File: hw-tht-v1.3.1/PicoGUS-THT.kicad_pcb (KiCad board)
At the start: 2 copper layers, 103.7 x 99.8 mm, 83 parts, among them J1 IRQDMA_JP, J10 GY-PCM5102, J3 Bus_ISA_8bit, J5 SJ1-3535NG, J6 UART_TX, J7 USB power jumper, J8 SJ1-3535NG-GR, J9 Waveblaster, U1 Pico, U10 74AHCT126, U11 NE5532, U2 74AHC244, U3 SN74CB3T3257, U4 SN74CB3T3257, U5 74AHC14, U6 74AHC00, U7 74AHC00, U8 APS6404L-3SQR-SN, U9 PCM5100A

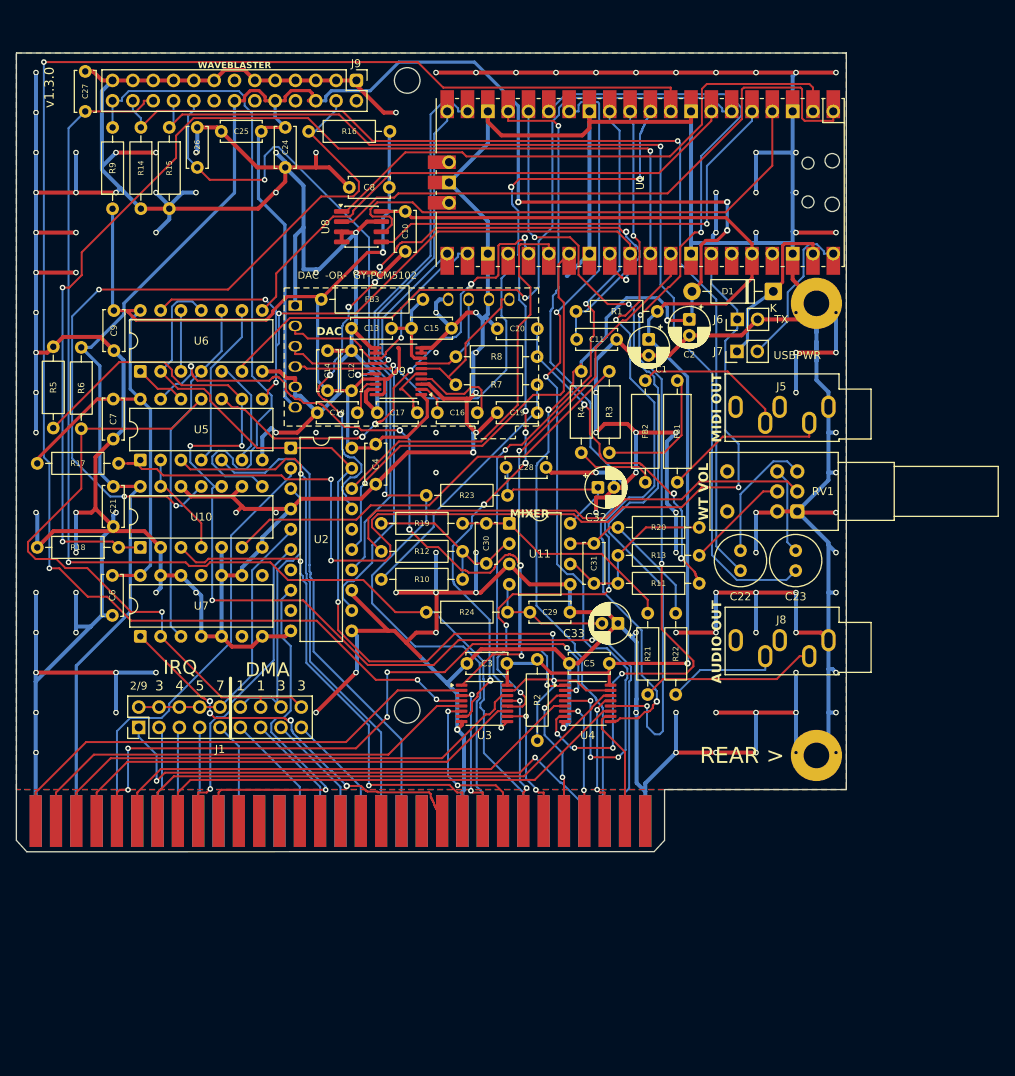
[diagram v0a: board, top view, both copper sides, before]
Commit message: THT rev B: dual USB-A/USB-C footprint, unrouted v1.3.1 board
- J11 footprint USB_A_C_Dual_Molex_67643_GCT_USB4085_Horizontal: Molex 67643
  USB-A or GCT USB4085 USB-C (all THT), both centred on one line, front faces
  1.5 mm beyond the board edge
- project rules: min hole-to-hole 0.45 mm, min annular 0.12 mm for the
  USB4085 pins; PicoGUS-THT.kicad_dru keeps 0.50/0.13 mm everywhere else
- PicoGUS-THT.kicad_pcb: unrouted (tracks, vias and zone fills removed),
  v1.3.0 positions; U1 on RPi_Pico_SMD_TH_USB, U3/U4 on the nested footprint
  at their old centres (turned 90 deg), new parts parked below the ISA edge,
  J11 aligned to the bracket edge line; silkscreen v1.3.1
- schematic: J11 footprint, F1 Bourns MF-R050

Still to come: BOM, socket BOM, README.

Co-Authored-By: Claude Opus 5.5 <noreply@anthropic.com>
Claude-Session: https://claude.ai/code/session_011utN3x8yYUNDvkpGCEq5yD
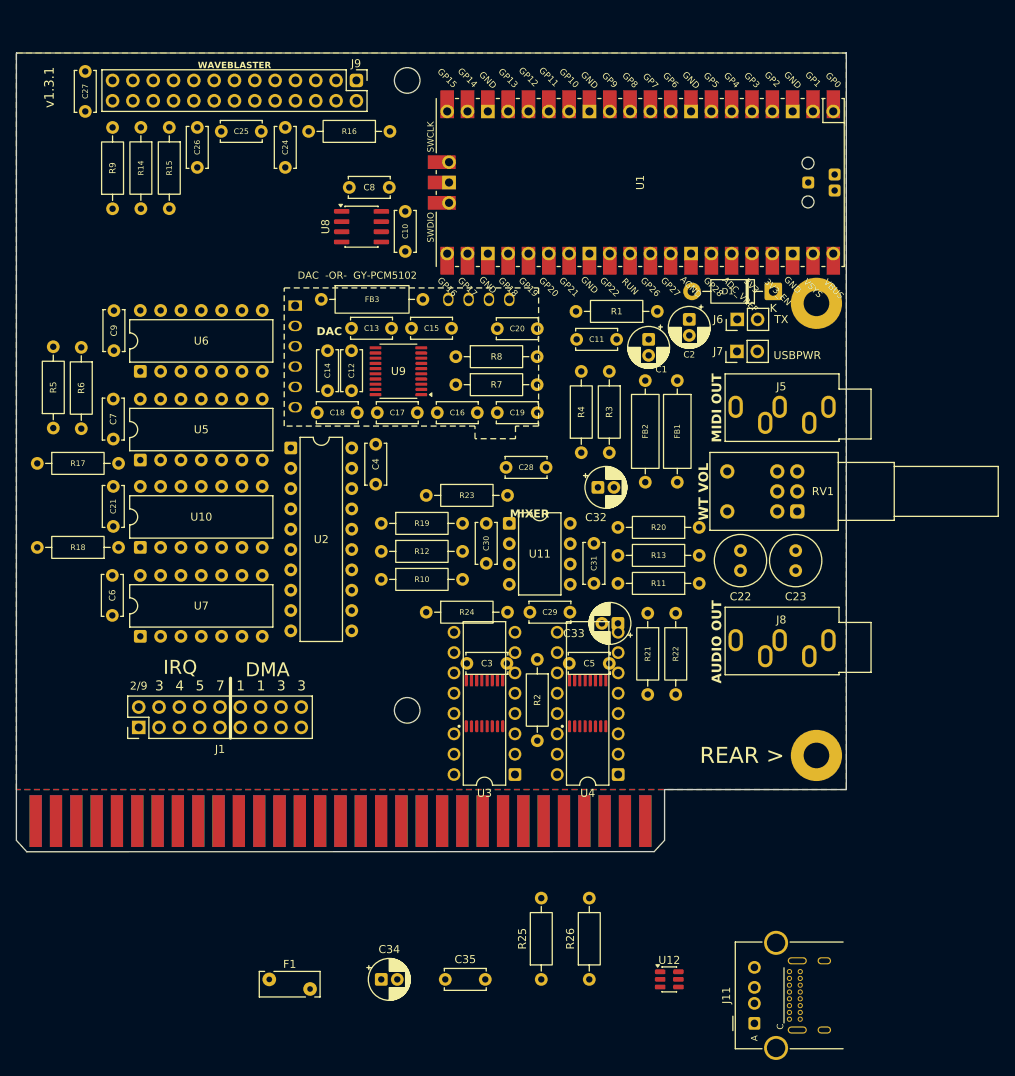
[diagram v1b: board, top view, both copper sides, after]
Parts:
- added C34: 47uF, Capacitor_THT:CP_Radial_D5.0mm_P2.00mm, F.Cu at (162.0, 152.0)
- added C35: 0.1uF, Capacitor_THT:C_Disc_D5.0mm_W2.5mm_P5.00mm, F.Cu at (170.0, 152.0)
- added F1: 0.5A PTC, Fuse:Fuse_Bourns_MF-RHT050, F.Cu at (148.0, 152.0)
- added J11: USB-A or USB-C, PiGUS library:USB_A_C_Dual_Molex_67643_GCT_USB4085_Horizontal, F.Cu at (220.1, 154.0)
- added R25: 56K, Resistor_THT:R_Axial_DIN0207_L6.3mm_D2.5mm_P10.16mm_Horizontal, F.Cu at (182.0, 152.0)
- added R26: 56K, Resistor_THT:R_Axial_DIN0207_L6.3mm_D2.5mm_P10.16mm_Horizontal, F.Cu at (188.0, 152.0)
- added U12: USBLC6-2SC6, Package_TO_SOT_SMD:SOT-23-6, F.Cu at (198.0, 152.0)
- U1: footprint PiGUS library:RPi_Pico_SMD_TH -> PiGUS library:RPi_Pico_SMD_TH_USB
- U3, U4: footprint Package_SO:TSSOP-16_4.4x5mm_P0.65mm -> PiGUS library:DIP-16_W7.62mm_TSSOP-16_Nested
- turned U3 to 90 degrees
- turned U4 to 90 degrees
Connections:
- J10 pad 13: /PCM5100 audio/DAC_OUTR -> /PCM5100 audio/AUDIO_R
- J10 pad 15: /PCM5100 audio/DAC_OUTL -> /PCM5100 audio/AUDIO_L
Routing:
- net GND: track 1290.5 -> 0.00 mm, vias 131 -> 0
- net +5V: track 335.3 -> 0.00 mm, vias 5 -> 0
- net +3V3: track 317.7 -> 0.00 mm, vias 2 -> 0
- net AD0: track 204.6 -> 0.00 mm, vias 4 -> 0
- net ADS: track 156.5 -> 0.00 mm, vias 7 -> 0
- net -12V: track 146.3 -> 0.00 mm, vias 1 -> 0
- net ~{RI/OCHRDY}: track 141.9 -> 0.00 mm, vias 3 -> 0
- net RESET: track 141.2 -> 0.00 mm, vias 4 -> 0
- net AD5: track 134.1 -> 0.00 mm, vias 7 -> 0
- net /Wavetable & line out/WT_R: track 133.3 -> 0.00 mm, vias 1 -> 0
- net UART_TX: track 132.5 -> 0.00 mm, vias 3 -> 0
- net +12V: track 130.8 -> 0.00 mm, vias 2 -> 0
- net /Wavetable & line out/WT_L: track 130.2 -> 0.00 mm, vias 1 -> 0
- net ~{BUSOE}: track 121.6 -> 0.00 mm, vias 3 -> 0
- net AD4: track 109.7 -> 0.00 mm, vias 5 -> 0
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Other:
- board text added: "PicoGUS v1.3.1 © 2023-2026 Ian Scott (polpo), Vidar Waagbø (waagbo) Licensed under CERN-OHL-P v2 https://github.com/waagbo/picogus Thanks to all the people that have contributed over the years!"
- board text added: "rev B (v1.3.1) new parts, to be placed: J11 USB-A/C: origin on the bracket edge line, rot 90 (aligned already) F1, C34, C35 near J11; R25/R26 USB-C CC; U12 ESD (optional)"
- board text added: "v1.3.1"
- board text removed: "PicoGUS v1.3.0 © 2023-2026 Ian Scott (polpo), Vidar Waagbø (waagbo) Licensed under CERN-OHL-P v2 https://github.com/waagbo/picogus Thanks to all the people that have contributed over the years!"
- board text removed: "v1.3.0"

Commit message: THT rev B: review fixes, C34 220uF, schematic PDF
Schematic
- C34 (USB VBUS bulk) 220 uF low-impedance Rubycon 16ZLH220MEFC6.3X11
  (USB 2.0 asks for >= 120 uF per host port)
- own UUID namespace for the rev B items (the USB sheet had reused UUIDs of
  v1.3.0 items, which mixed up ERC markers)
- TP1-TP3 pin names empty ("") in the embedded Pico_USB copy (KiCad 10 drew
  "~" literally)
- R25/R26 DigiKey/LCSC fields, U3/U4 adapter note (PA0034C first, BOB-13994
  has 0.635 mm pads), U12 in the title block's SMD list, USB sheet note
  reworded, USB-C always-on VBUS warning
- schematic PDF re-exported (4 pages)

Board
- U1: the library footprint's Pico pin-name/SWD silkscreen texts removed
  again (as in the v1.3.0 label clean-up)
- U3/U4 references back at their v1.3.0 spots (were on the gold fingers)
- U1, U3, U4 back in their footprint groups
- VBUS_USB in the pwr net class

BOM: C34 own line; BOM, uploads and socket BOM regenerated.

Co-Authored-By: Claude Opus 5.5 <noreply@anthropic.com>
Claude-Session: https://claude.ai/code/session_011utN3x8yYUNDvkpGCEq5yD
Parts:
- C34: value 47uF -> 220uF; footprint Capacitor_THT:CP_Radial_D5.0mm_P2.00mm -> Capacitor_THT:CP_Radial_D6.3mm_P2.50mm

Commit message: THT rev B: USB-A only for J11 (USB-C on hold)
- J11: Connector:USB_A on the stock Connector_USB:USB_A_Molex_67643_Horizontal
  (Molex 0676430910), parked with the flange 1.5 mm beyond the bracket edge
- R25/R26 (USB-C CC Rp) removed; design rules back to v1.3.0 (min hole-to-hole
  0.50 mm, annular 0.13 mm), PicoGUS-THT.kicad_dru removed
- the dual USB-A/USB-C footprint stays in the shared library, unused, for a
  possible USB-C option later
- BOM, DigiKey uploads, schematic PDF and README updated

Co-Authored-By: Claude Opus 5.5 <noreply@anthropic.com>
Claude-Session: https://claude.ai/code/session_011utN3x8yYUNDvkpGCEq5yD
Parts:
- removed R25, R26: 56K, Resistor_THT:R_Axial_DIN0207_L6.3mm_D2.5mm_P10.16mm_Horizontal
- J11: value USB-A or USB-C -> USB-A; footprint PiGUS library:USB_A_C_Dual_Molex_67643_GCT_USB4085_Horizontal -> Connector_USB:USB_A_Molex_67643_Horizontal
- moved U12 16.0 mm to (182.0, 152.0)
- moved J11 12.0 mm to (208.6, 157.5)
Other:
- board text added: "rev B (v1.3.1) new parts, to be placed: J11 USB-A: flange 1.5 mm beyond the bracket edge (aligned already) F1, C34, C35 near J11; U12 ESD (optional)"
- board text removed: "rev B (v1.3.1) new parts, to be placed: J11 USB-A/C: origin on the bracket edge line, rot 90 (aligned already) F1, C34, C35 near J11; R25/R26 USB-C CC; U12 ESD (optional)"

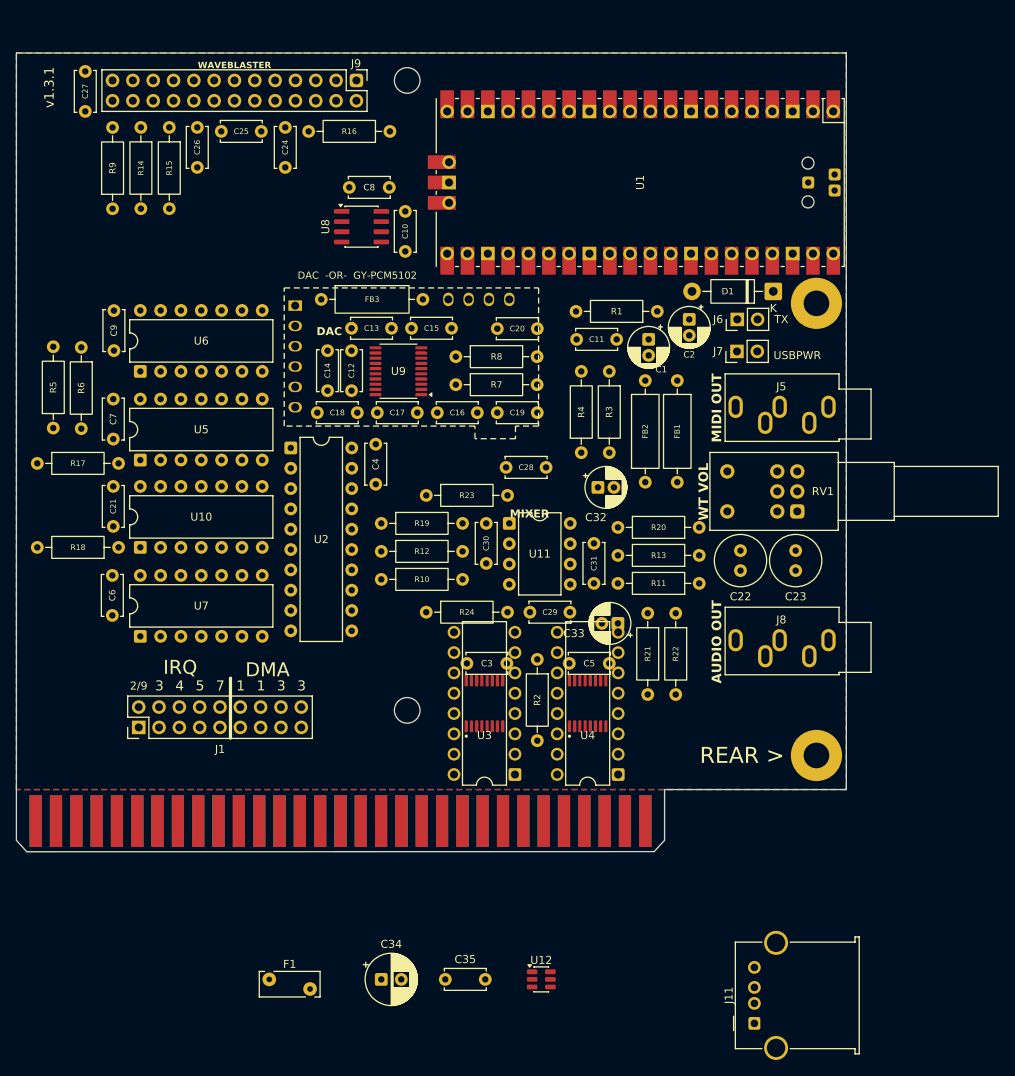
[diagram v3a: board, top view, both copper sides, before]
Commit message: THT rev B: user's new placement; USB port and Waveblaster standoff holes dropped
- PicoGUS-THT.kicad_pcb: the user's rev B placement (Pico moved down, bracket
  parts and mixer regrouped), unrouted
- USB host port removed again (usb.kicad_sch, J11, F1, C34, C35, U12); U1 back
  on the v1.3.0 Pico symbol and RPi_Pico_SMD_TH footprint
- J9 on the new Wavetable_NoMountingHoles footprint (no daughterboard standoff
  holes; the far one landed in U4); standoff and screws dropped from the BOM
- card outline: the 6.35 mm Edge.Cuts step at x 197.41 next to the ISA
  fingers had been dragged off the board in the upload; restored
- design rules identical to v1.3.0
- BOM, DigiKey uploads, socket BOM, schematic PDF and README updated

Co-Authored-By: Claude Opus 5.5 <noreply@anthropic.com>
Claude-Session: https://claude.ai/code/session_011utN3x8yYUNDvkpGCEq5yD
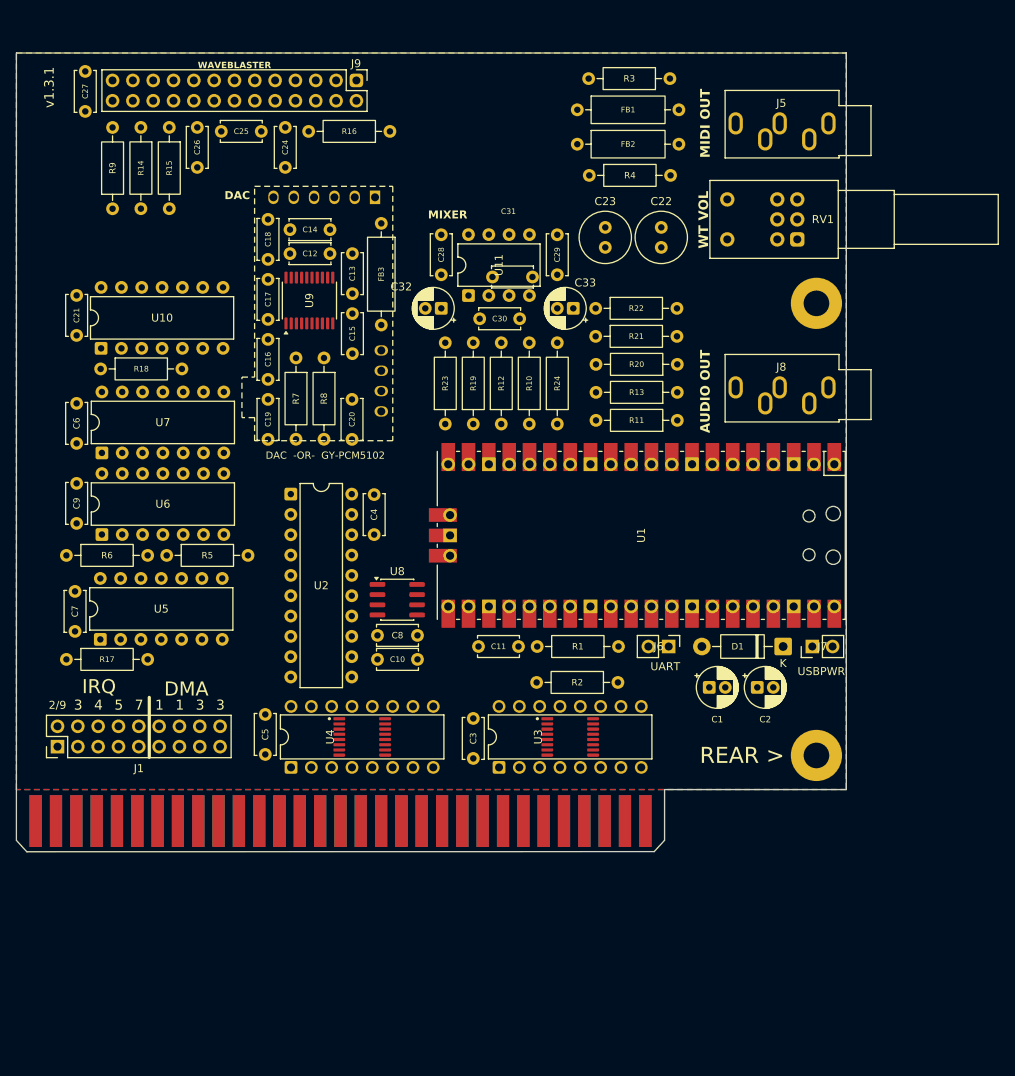
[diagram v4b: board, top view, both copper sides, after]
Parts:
- removed C34: 220uF, Capacitor_THT:CP_Radial_D6.3mm_P2.50mm
- removed C35: 0.1uF, Capacitor_THT:C_Disc_D5.0mm_W2.5mm_P5.00mm
- removed F1: 0.5A PTC, Fuse:Fuse_Bourns_MF-RHT050
- removed J11: USB-A, Connector_USB:USB_A_Molex_67643_Horizontal
- removed U12: USBLC6-2SC6, Package_TO_SOT_SMD:SOT-23-6
- J9: footprint PiGUS library:Wavetable -> PiGUS library:Wavetable_NoMountingHoles
- U1: footprint PiGUS library:RPi_Pico_SMD_TH_USB -> PiGUS library:RPi_Pico_SMD_TH
- moved C8 56.1 mm to (166.5, 109.0)
- moved C10 56.0 mm to (166.5, 112.0), turned to 180 degrees
- moved C23 49.1 mm to (190.0, 58.0), turned to -90 degrees
- moved C29 47.2 mm to (184.0, 58.9), turned to -90 degrees
- moved U8 46.8 mm to (164.0, 104.5)
- moved C2 46.8 mm to (209.0, 115.5), turned to 0 degrees
- moved D1 44.4 mm to (212.2, 110.4)
- moved C1 44.2 mm to (203.0, 115.5), turned to 0 degrees
- moved U1 44.1 mm to (194.5, 96.5)
- moved C22 44.0 mm to (197.0, 58.0), turned to -90 degrees
- moved C5 43.5 mm to (147.5, 118.9), turned to -90 degrees
- moved FB2 43.1 mm to (186.5, 47.6), turned to 0 degrees
- moved R1 42.2 mm to (191.7, 110.4)
- moved J6 41.8 mm to (197.9, 110.4), turned to -90 degrees
- moved C33 39.8 mm to (186.0, 68.1)
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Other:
- board text added: "UART"
- board text removed: "TX"
- board text removed: "rev B (v1.3.1) new parts, to be placed: J11 USB-A: flange 1.5 mm beyond the bracket edge (aligned already) F1, C34, C35 near J11; U12 ESD (optional)"

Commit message: THT rev B: take 2 placement with the USB-A port back; C31 above U11
- PicoGUS-THT.kicad_pcb: the user's take-2 placement (USB-A J11 at the
  bracket, Pico lower, RV1/J8/J5/J11 down the bracket, U3/U4 upright),
  unrouted; J9 on Wavetable_NoMountingHoles; C31 moved to (177, 40.5) above
  U11 (was inside its DIP body); the dragged Edge.Cuts step at x 197.41
  restored again
- schematic: USB host port sheet and the Pico with USB test points back,
  J9 without standoff holes; VBUS_USB in the pwr net class
- BOM, DigiKey uploads, socket BOM, schematic PDF and README for the USB-A
  version (Pico soldered flat, no daughterboard standoff)

Co-Authored-By: Claude Opus 5.5 <noreply@anthropic.com>
Claude-Session: https://claude.ai/code/session_011utN3x8yYUNDvkpGCEq5yD
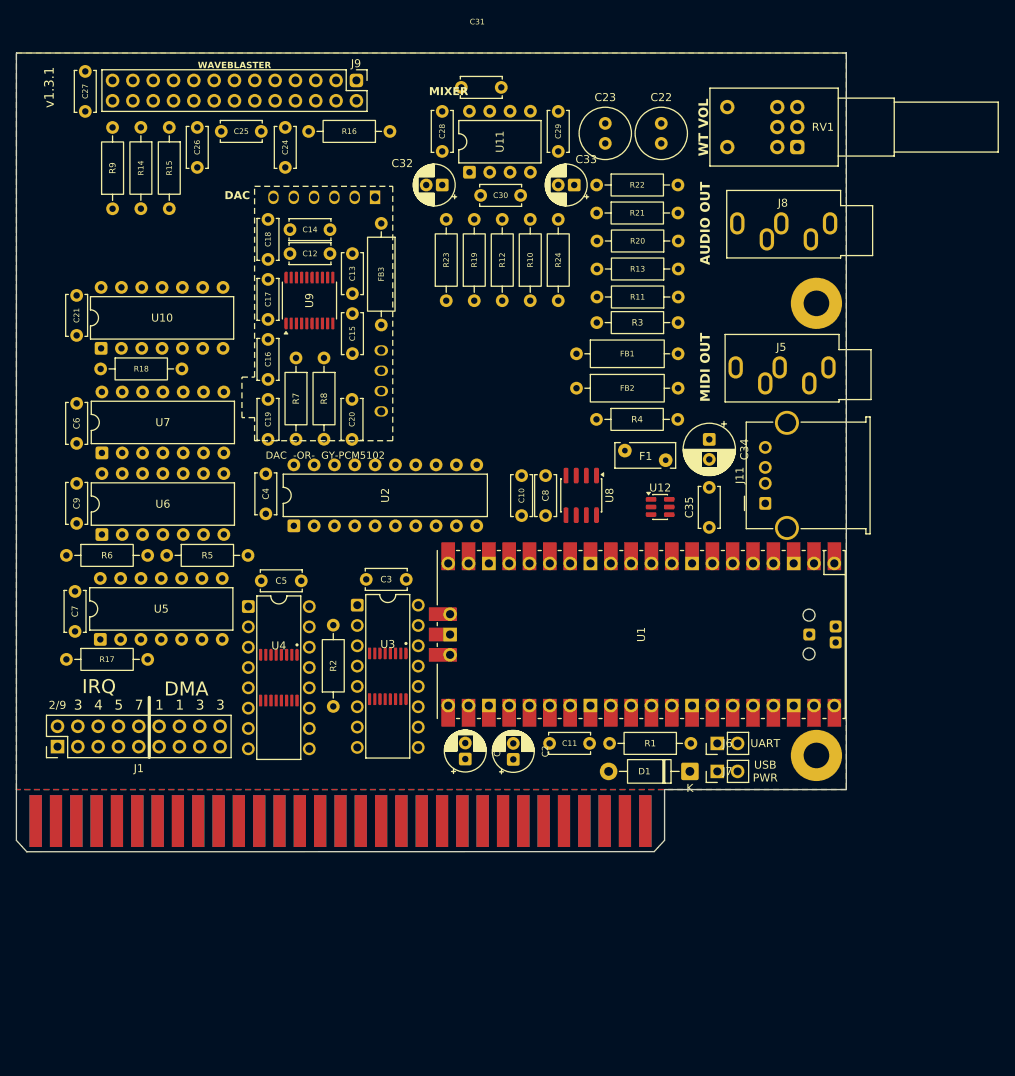
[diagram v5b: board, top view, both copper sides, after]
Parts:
- added C34: 220uF, Capacitor_THT:CP_Radial_D6.3mm_P2.50mm, F.Cu at (203.0, 84.5)
- added C35: 0.1uF, Capacitor_THT:C_Disc_D5.0mm_W2.5mm_P5.00mm, F.Cu at (203.0, 95.5)
- added F1: 0.5A PTC, Fuse:Fuse_Bourns_MF-RHT050, F.Cu at (192.4, 85.9)
- added J11: USB-A, Connector_USB:USB_A_Molex_67643_Horizontal, F.Cu at (210.0, 92.5)
- added U12: USBLC6-2SC6, Package_TO_SOT_SMD:SOT-23-6, F.Cu at (196.9, 93.0)
- U1: footprint PiGUS library:RPi_Pico_SMD_TH -> PiGUS library:RPi_Pico_SMD_TH_USB
- moved R2 35.7 mm to (156.0, 117.9), turned to 90 degrees
- moved C2 31.8 mm to (178.5, 124.5), turned to 90 degrees
- moved C1 31.8 mm to (172.5, 124.5), turned to 90 degrees
- moved R3 30.5 mm to (199.1, 69.9)
- moved R4 30.5 mm to (188.9, 82.0)
- moved FB1 30.5 mm to (186.4, 73.8)
- moved FB2 30.5 mm to (186.4, 78.1)
- moved J5 30.5 mm to (217.9, 75.5)
- moved U8 26.4 mm to (187.0, 91.5), turned to -90 degrees
- moved U3 24.0 mm to (162.8, 114.1), turned to -90 degrees
- moved C31 24.0 mm to (177.0, 40.5)
- moved C10 22.2 mm to (179.5, 94.0), turned to 90 degrees
- moved C8 21.9 mm to (182.5, 94.0), turned to 90 degrees
- moved J8 20.5 mm to (218.1, 57.5)
- moved J7 19.6 mm to (204.0, 126.0)
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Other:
- board text added: "USB PWR"
- board text removed: "REAR >"
- board text removed: "USBPWR"
